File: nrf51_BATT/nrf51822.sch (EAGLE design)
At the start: 20 parts, among them T1 MMUN2238

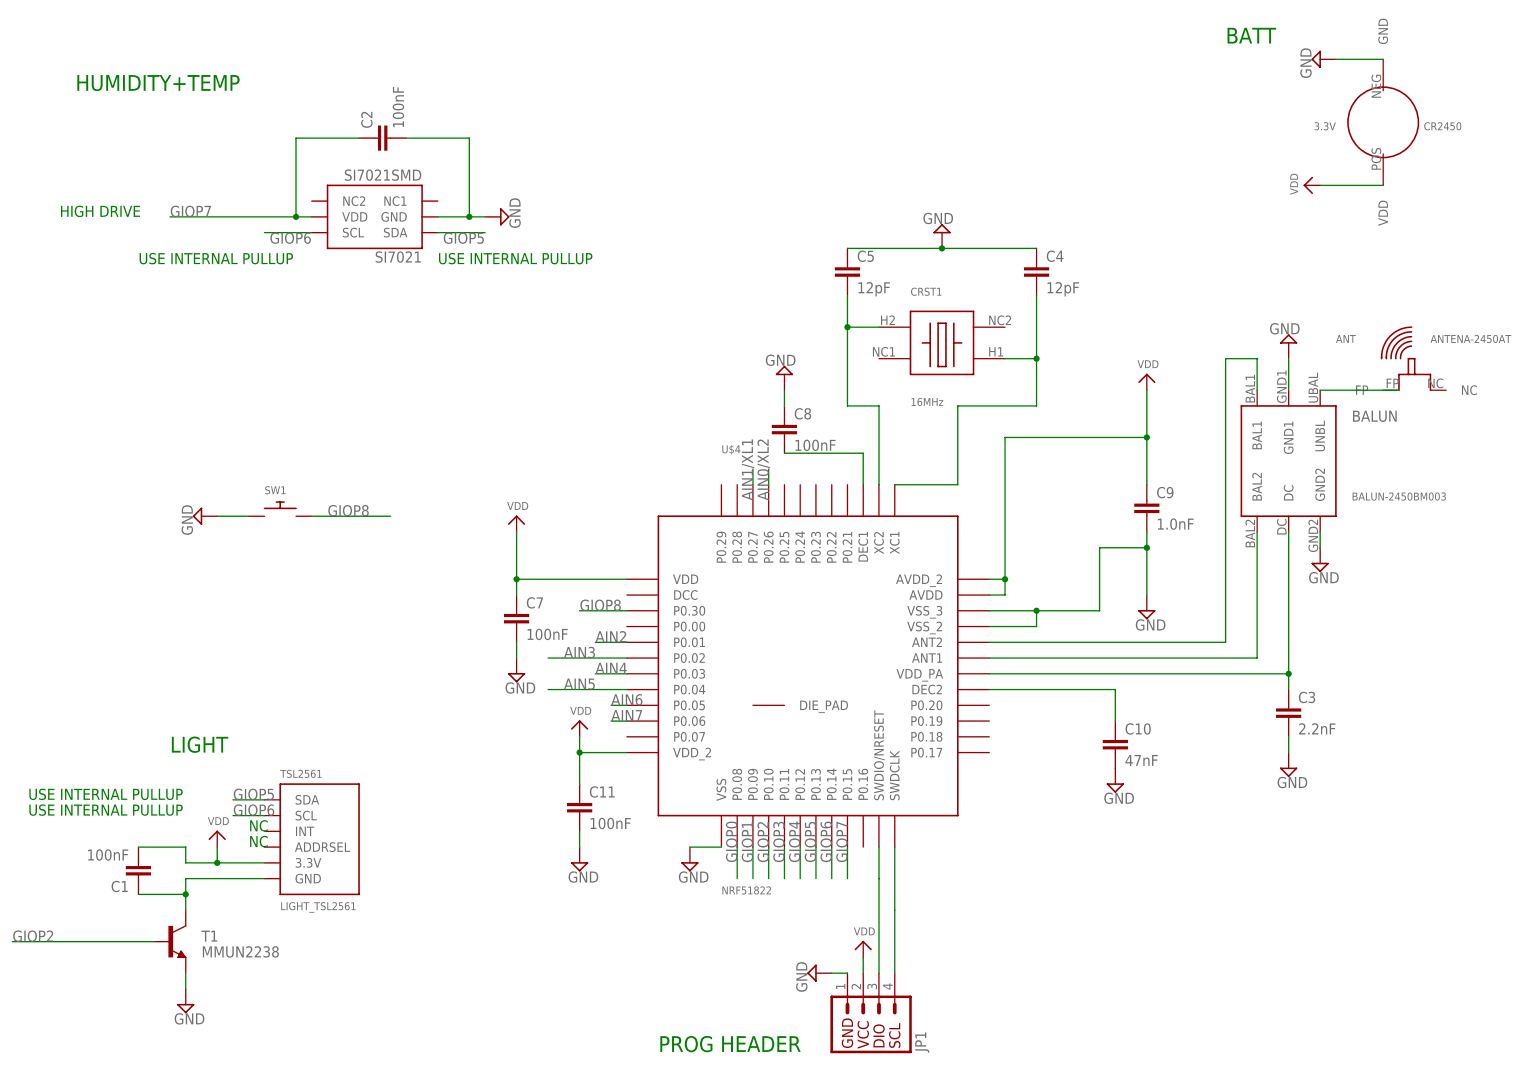
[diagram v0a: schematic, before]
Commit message: Cleaned sensor board v.1.2 - TAG AS SENT TO SMART PROTOTYPE Cleaned actuation board v.1.0 - TAG AS SENT TO SMART PROTOTYPE Made a compact version of the sensor board - TAG AS SENT TO SMART PROTOTYPE
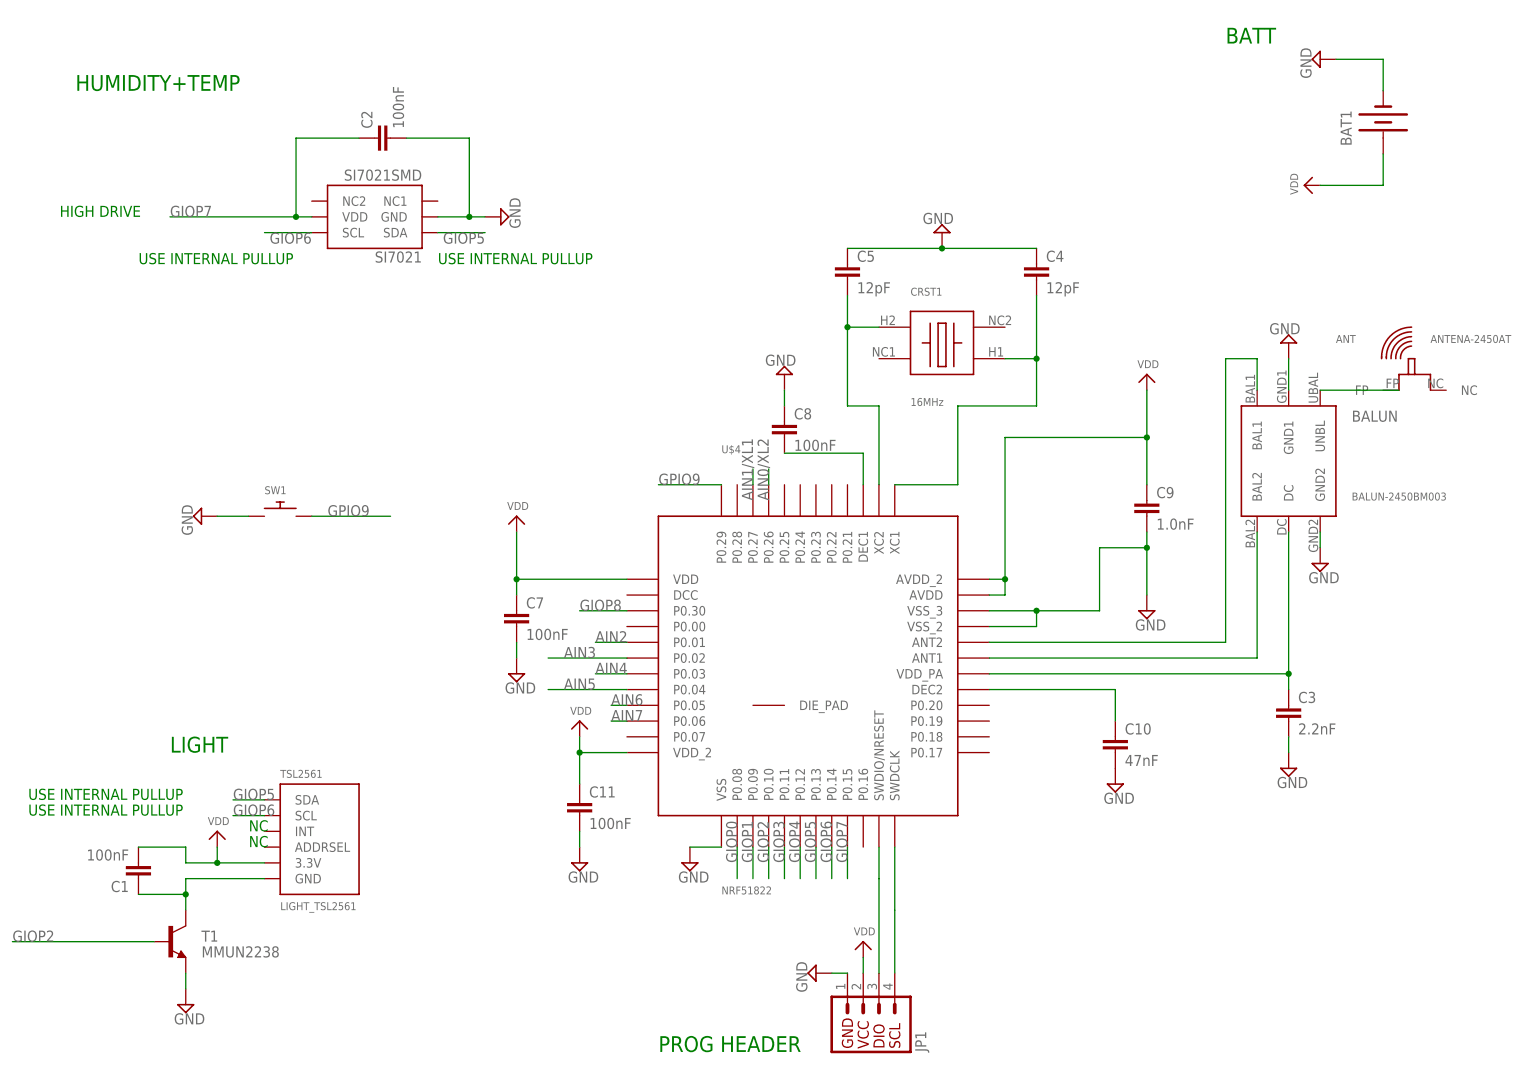
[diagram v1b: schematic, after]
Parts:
- removed CR2450: 3.3V, NordicSemi:CR2450
- added BAT1: (no value), SparkFun-Electromechanical:BATTERY245PTH
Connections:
- new net GPIO9: SW1.P$2, U$4.P0.29
- net GIOP8: no longer SW1.P$2
- net GND: now also BAT1.-
- net VDD: now also BAT1.+
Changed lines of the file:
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@@
 <schematic xreflabel="%F%N/%S.%C%R" xrefpart="/%S.%C%R">
 <attributes>
-<attribute name="CNAME" value="BLEoT"/>
-<attribute name="CREVISION" value="1.2"/>
+<attribute name="CNAME" value="BLEoT COMPACT"/>
+<attribute name="CREVISION" value="1.0"/>
 <attribute name="DESIGNER" value="Mohammed Aljarrah"/>
 </attributes>
@@
 <part name="BG" library="microbuilder" deviceset="VDD" device=""/>
 <part name="U$5" library="microbuilder" deviceset="VDD" device=""/>
-<part name="CR2450" library="NordicSemi" deviceset="CR2450" device="" value="3.3V"/>
 <part name="TSL2561" library="microbuilder" deviceset="LIGHT_TSL2561" device=""/>
 <part name="C1" library="rcl" deviceset="C-EU" device="C0805" value="100nF"/>
@@
 <part name="C4" library="rcl" deviceset="C-EU" device="C0805" value="12pF"/>
 <part name="C5" library="rcl" deviceset="C-EU" device="C0805" value="12pF"/>
+<part name="BAT1" library="SparkFun-Electromechanical" deviceset="BATTERY" device="245PTH"/>
 </parts>
 <sheets>
@@
 <instance part="BG" gate="G$1" x="109.22" y="93.98"/>
 <instance part="U$5" gate="G$1" x="17.78" y="38.1"/>
-<instance part="CR2450" gate="G$1" x="147.32" y="134.62" rot="R180"/>
 <instance part="TSL2561" gate="G$1" x="-22.86" y="20.32"/>
 <instance part="C1" gate="G$1" x="-53.34" y="12.7" rot="R180"/>
@@
 <instance part="C4" gate="G$1" x="91.44" y="111.76"/>
 <instance part="C5" gate="G$1" x="60.96" y="111.76"/>
+<instance part="BAT1" gate="G$1" x="147.32" y="134.62" rot="R90"/>
 </instances>
 <busses>
@@
 <pinref part="SUPPLY4" gate="GND" pin="GND"/>
 <wire x1="147.32" y1="144.78" x2="139.7" y2="144.78" width="0.1" layer="91"/>
+<pinref part="BAT1" gate="G$1" pin="-"/>
+<wire x1="147.32" y1="144.78" x2="147.32" y2="139.7" width="0.1" layer="91"/>
 </segment>
 <segment>
@@
 <pinref part="AA" gate="G$1" pin="VDD"/>
 <wire x1="137.16" y1="124.46" x2="147.32" y2="124.46" width="0.1524" layer="91"/>
+<pinref part="BAT1" gate="G$1" pin="+"/>
+<wire x1="147.32" y1="129.54" x2="147.32" y2="124.46" width="0.1" layer="91"/>
 </segment>
 <segment>
@@
 <wire x1="25.4" y1="55.88" x2="17.78" y2="55.88" width="0.1" layer="91"/>
 <label x="17.78" y="55.88" size="1.778" layer="95"/>
-</segment>
-<segment>
-<pinref part="SW1" gate="G$1" pin="P$2"/>
-<wire x1="-25.4" y1="71.12" x2="-12.7" y2="71.12" width="0.1" layer="91"/>
-<label x="-22.86" y="71.12" size="1.778" layer="95"/>
 </segment>
 </net>
@@
 </segment>
 </net>
+<net name="GPIO9" class="0">
+<segment>
+<pinref part="U$4" gate="G$1" pin="P0.29"/>
+<wire x1="40.64" y1="76.2" x2="30.48" y2="76.2" width="0.1" layer="91"/>
+<label x="30.48" y="76.2" size="1.778" layer="95"/>
+</segment>
+<segment>
+<pinref part="SW1" gate="G$1" pin="P$2"/>
+<wire x1="-25.4" y1="71.12" x2="-12.7" y2="71.12" width="0.1" layer="91"/>
+<label x="-22.86" y="71.12" size="1.778" layer="95"/>
+</segment>
+</net>
